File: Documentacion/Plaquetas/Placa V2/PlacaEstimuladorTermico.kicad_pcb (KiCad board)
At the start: 2 copper layers, 207.5 x 149.9 mm, 72 parts, among them J1 Conn_01x02, J10 Conn_01x04_Male, J2 DB9_Female_MountingHoles, J3 Conn_01x01, J4 Conn_01x01, J5 Conn_01x02, J6 Pulsador OFF, J7 Conn_02x05_Counter_Clockwise, J8 Conn_02x05_Counter_Clockwise, J9 Conn_01x04_Male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

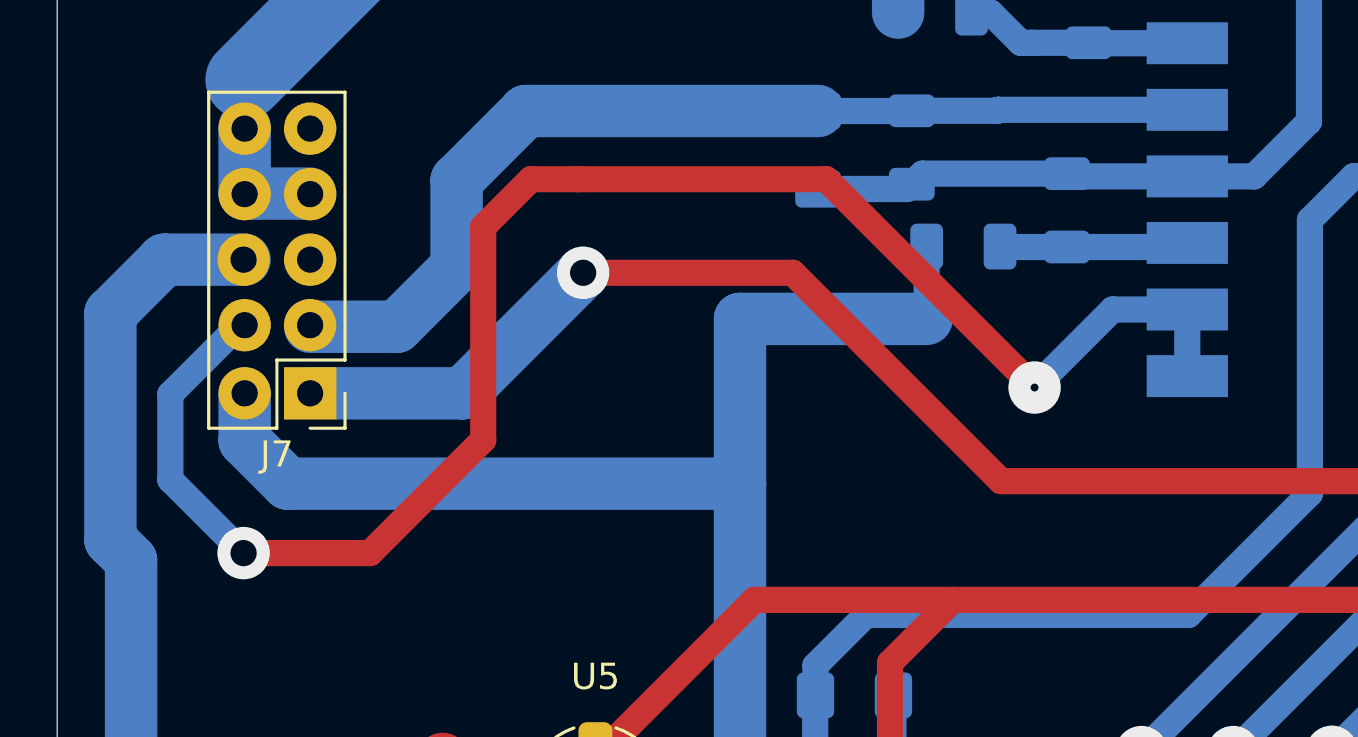
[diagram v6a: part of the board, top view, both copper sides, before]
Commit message: simplification of the dissipator temperature measurement circuit and simplification of code
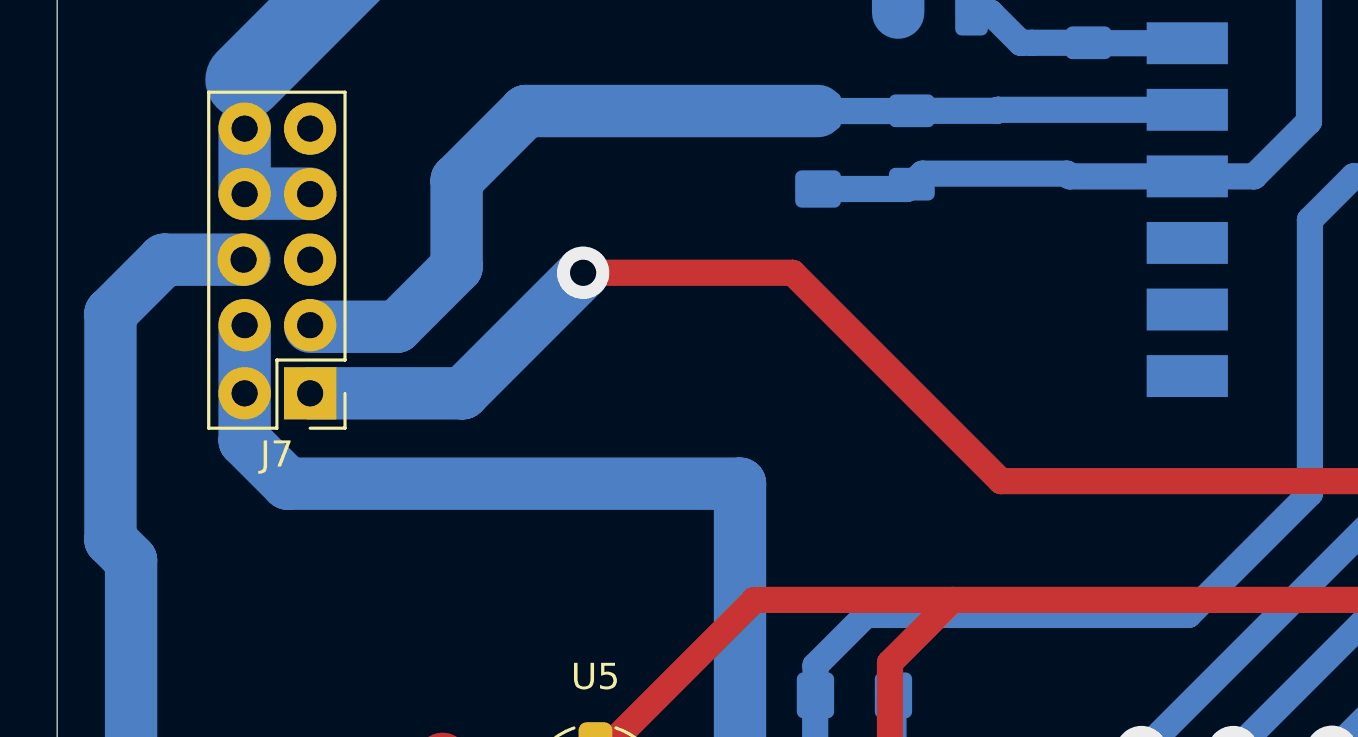
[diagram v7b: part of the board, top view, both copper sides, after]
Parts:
- removed R6: 3.3k, Resistor_SMD:R_1206_3216Metric
- removed R7: 1k, Resistor_SMD:R_1206_3216Metric
- C11: value 4.7n -> 47n
- R10: value 68k -> 10k
- R8: value 39k -> 10k
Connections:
- J7 pad 9: term_disip_1 -> REF_OPAMPS
- U1 pad 10: Net-(R6-Pad2) -> (no net)
- U1 pad 8: term_disip_1 -> (no net)
- U1 pad 9: term_disip_1 -> (no net)
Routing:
- net term_disip_1: track 64.8 -> 0.00 mm, vias 2 -> 0
- net REF_OPAMPS: track 57.6 -> 44.2 mm
- net Net-(R6-Pad2): track 7.22 -> 0.00 mm

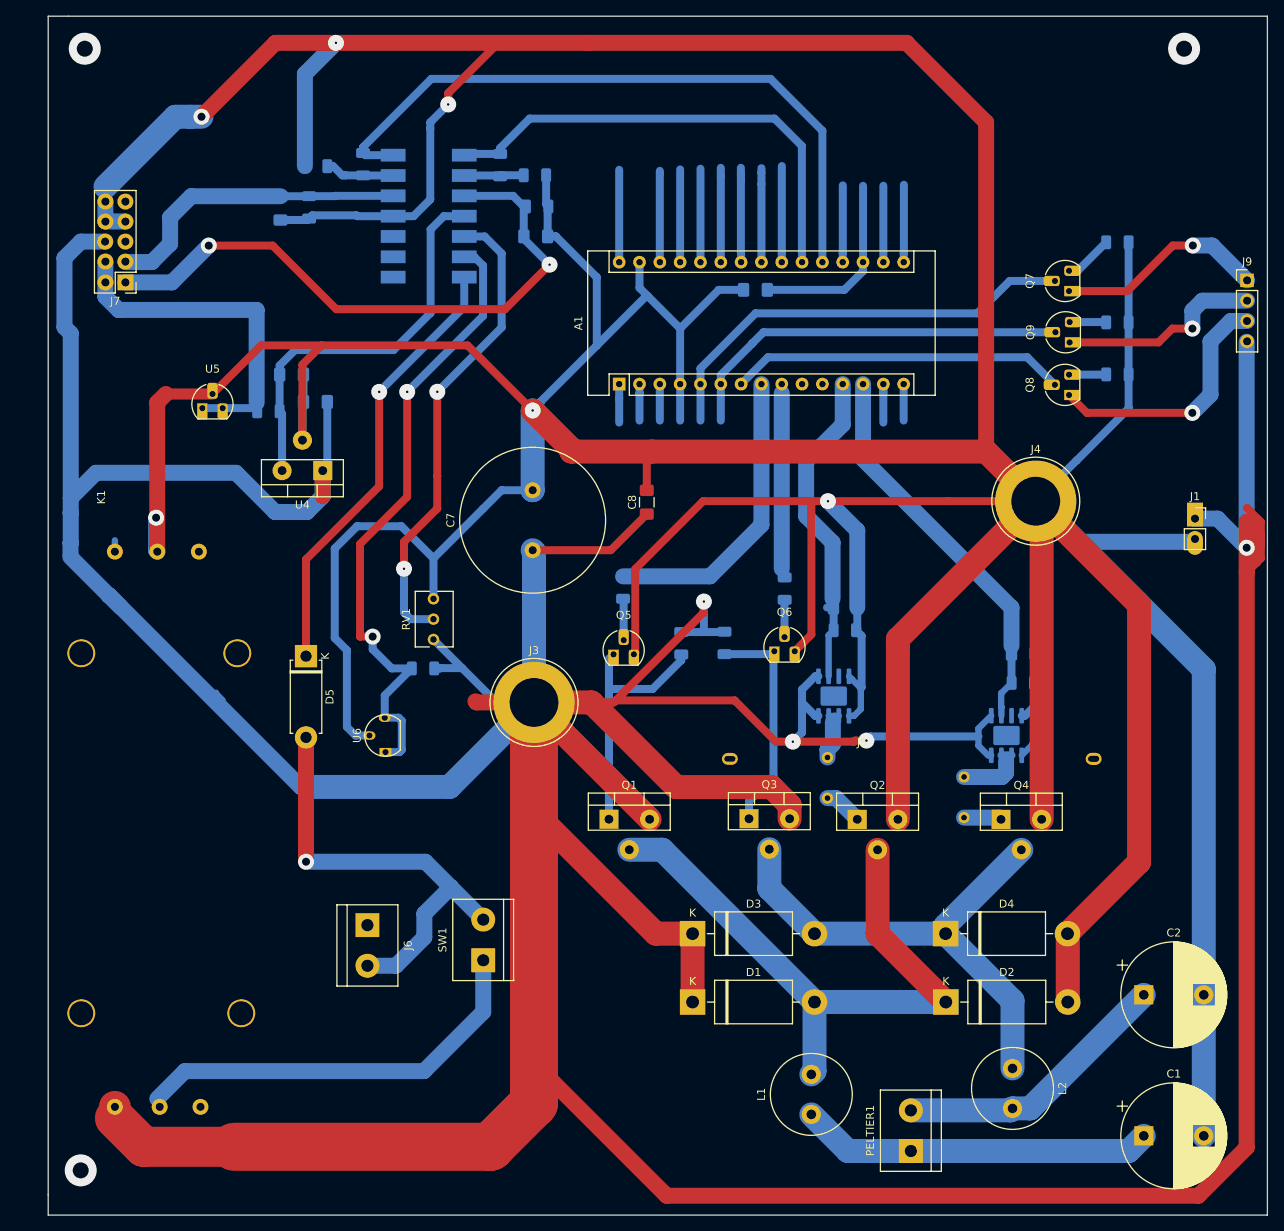
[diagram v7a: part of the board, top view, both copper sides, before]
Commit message: Add fuse and 7805 to supply the arduino nano
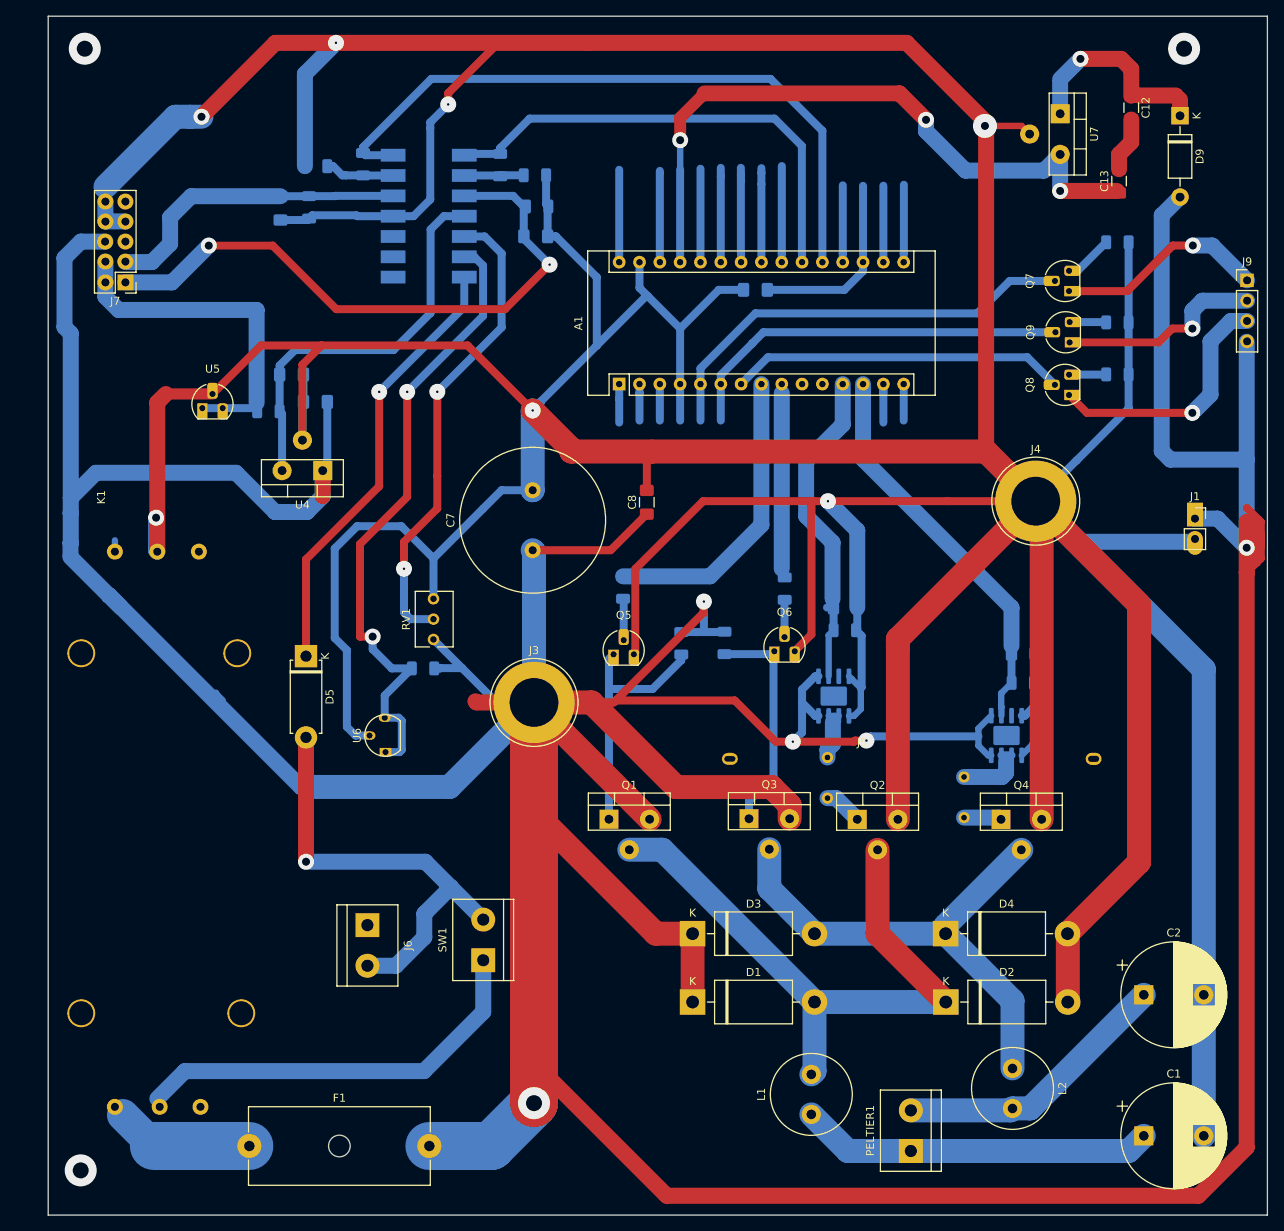
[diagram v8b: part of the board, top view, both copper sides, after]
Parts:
- added C12: 0.33u, Capacitor_SMD:C_1206_3216Metric_Pad1.42x1.75mm_HandSolder, F.Cu at (247.1, 24.1)
- added C13: 0.1u, Capacitor_SMD:C_1206_3216Metric_Pad1.42x1.75mm_HandSolder, F.Cu at (245.6, 33.3)
- added D9: 1N4002, Diode_THT:D_DO-41_SOD81_P10.16mm_Horizontal, F.Cu at (253.2, 25.1)
- added F1: Fuse, Fuse:Fuseholder_Cylinder-5x20mm_Schurter_0031_8201_Horizontal_Open, F.Cu at (136.9, 153.9)
- added U7: L7805, custom_footprints:TO-220-3_Vertical, F.Cu at (238.3, 24.9)
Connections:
- K1 pad 4: VCC -> Net-(F1-Pad1)
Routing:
- net Net-(A1-Pad27): track 11.6 -> 84.8 mm, vias 0 -> 3
- net Net-(C12-Pad1): track 0.00 -> 26.5 mm, vias 0 -> 1
- net Net-(F1-Pad1): track 0.00 -> 18.8 mm
- net Net-(C12-Pad2): track 0.00 -> 6.84 mm
- net GND: track 1016.9 -> 1022.9 mm, vias 6 -> 7
- net VCC: track 781.0 -> 782.5 mm, vias 4 -> 5
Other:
- outline, holes or cut-outs redrawn
